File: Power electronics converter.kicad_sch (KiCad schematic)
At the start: 0 parts

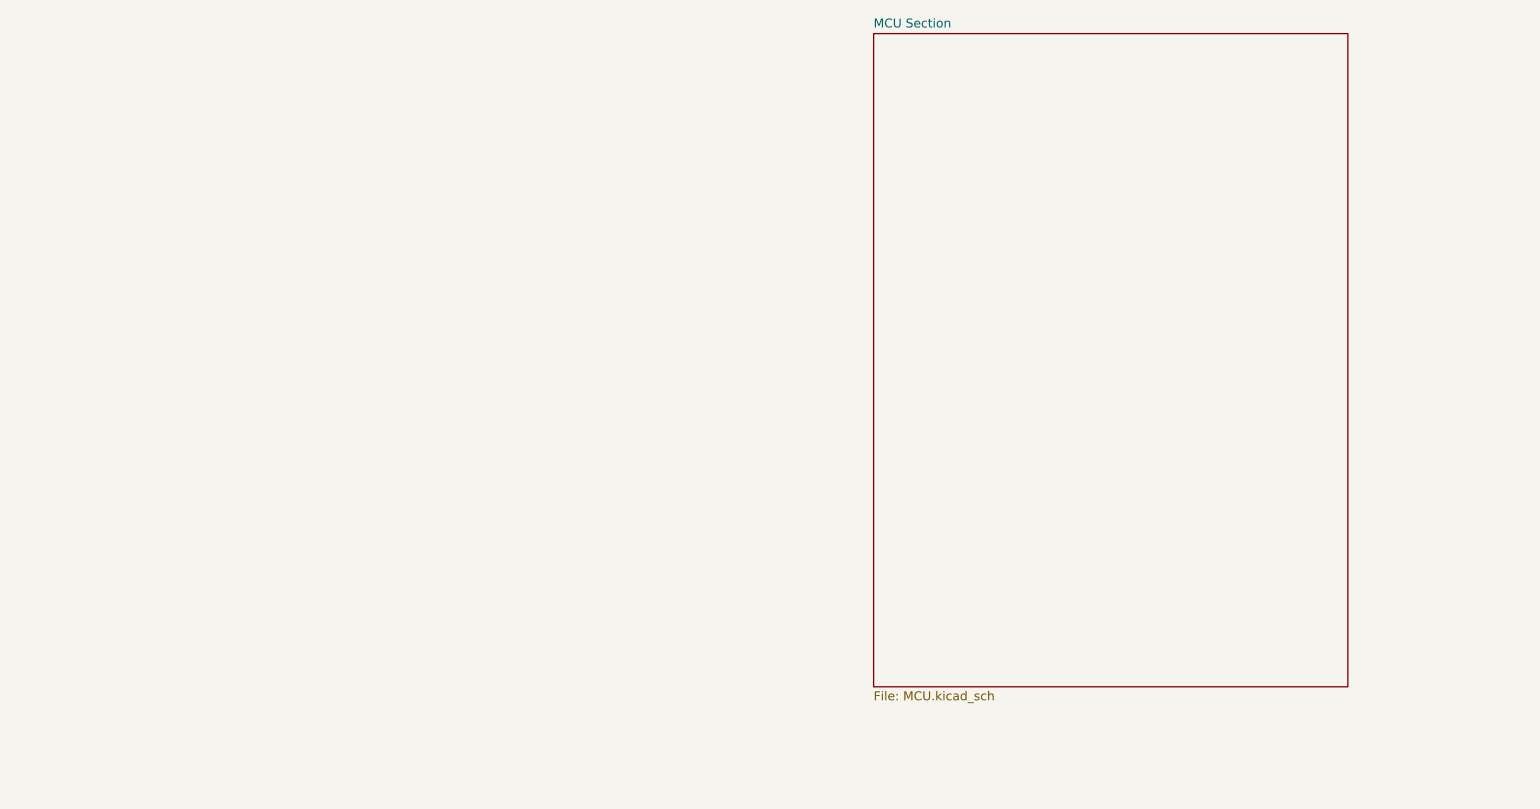
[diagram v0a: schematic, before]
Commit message: Schematic finished pending of layout
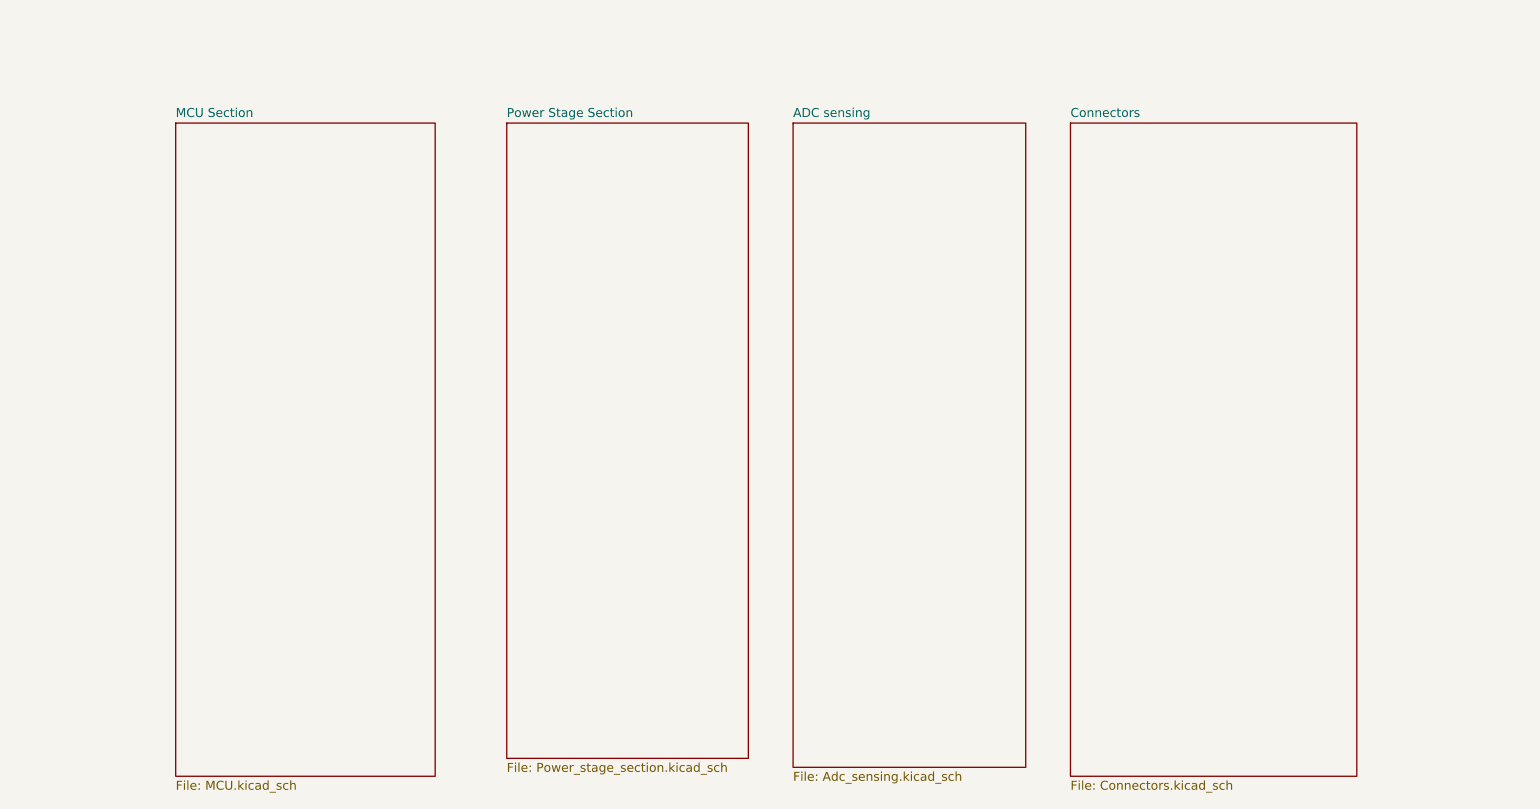
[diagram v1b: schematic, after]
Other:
- added sheet ADC sensing (Adc_sensing.kicad_sch)
- added sheet Connectors (Connectors.kicad_sch)
- added sheet Power Stage Section (Power_stage_section.kicad_sch)
- title: (none) -> SYNCHRONOUS BUCK CONVERTER PROJECT
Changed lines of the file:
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@@
 	(generator_version "9.0")
 	(paper "A4")
+	(title_block
+		(title "SYNCHRONOUS BUCK CONVERTER PROJECT")
+	)
 	(sheet
-		(at 162.56 27.94)
-		(size 67.31 92.71)
+		(at 63.5 40.64)
+		(size 36.83 92.71)
 		(exclude_from_sim no)
 		(in_bom yes)
@@
 		)
 		(property "Sheetname" "MCU Section"
-			(at 162.56 27.2284 0)
+			(at 63.5 39.9284 0)
 			(effects
 				(font
@@
 		)
 		(property "Sheetfile" "MCU.kicad_sch"
-			(at 162.56 121.2346 0)
+			(at 63.5 133.9346 0)
 			(effects
 				(font
@@
 				)
 			)
+		)
+	)
+	(sheet
+		(at 151.13 40.64)
+		(size 33.02 91.44)
+		(exclude_from_sim no)
+		(in_bom yes)
+		(on_board yes)
+		(dnp no)
+		(fields_autoplaced yes)
+		(stroke
+			(width 0.1524)
+			(type solid)
+		)
+		(fill
+			(color 0 0 0 0.0000)
+		)
+		(property "Sheetname" "ADC sensing"
+			(at 151.13 39.9284 0)
+			(effects
+				(font
+					(size 1.27 1.27)
+				)
+				(justify left bottom)
+			)
+		)
+		(property "Sheetfile" "Adc_sensing.kicad_sch"
+			(at 151.13 132.6646 0)
+			(effects
+				(font
+					(size 1.27 1.27)
+				)
+				(justify left top)
+			)
+		)
+		(instances
+			(project "Power electronics converter"
+				(path "/8bff22cb-9bb1-47e8-8b56-bb93bafcd2ef"
+					(page "4")
+				)
+			)
+		)
+	)
+	(sheet
+		(at 190.5 40.64)
+		(size 40.64 92.71)
+		(exclude_from_sim no)
+		(in_bom yes)
+		(on_board yes)
+		(dnp no)
+		(fields_autoplaced yes)
+		(stroke
+			(width 0.1524)
+			(type solid)
+		)
+		(fill
+			(color 0 0 0 0.0000)
+		)
+		(property "Sheetname" "Connectors"
+			(at 190.5 39.9284 0)
+			(effects
+				(font
+					(size 1.27 1.27)
+				)
+				(justify left bottom)
+			)
+		)
+		(property "Sheetfile" "Connectors.kicad_sch"
+			(at 190.5 133.9346 0)
+			(effects
+				(font
+					(size 1.27 1.27)
+				)
+				(justify left top)
+			)
+		)
+		(instances
+			(project "Power electronics converter"
+				(path "/8bff22cb-9bb1-47e8-8b56-bb93bafcd2ef"
+					(page "5")
+				)
+			)
+		)
+	)
+	(sheet
+		(at 110.49 40.64)
+		(size 34.29 90.17)
+		(exclude_from_sim no)
+		(in_bom yes)
+		(on_board yes)
+		(dnp no)
+		(fields_autoplaced yes)
+		(stroke
+			(width 0.1524)
+			(type solid)
+		)
+		(fill
+			(color 0 0 0 0.0000)
+		)
+		(property "Sheetname" "Power Stage Section"
+			(at 110.49 39.9284 0)
+			(effects
+				(font
+					(size 1.27 1.27)
+				)
+				(justify left bottom)
+			)
+		)
+		(property "Sheetfile" "Power_stage_section.kicad_sch"
+			(at 110.49 131.3946 0)
+			(effects
+				(font
+					(size 1.27 1.27)
+				)
+				(justify left top)
+			)
+		)
+		(instances
+			(project "Power electronics converter"
+				(path "/8bff22cb-9bb1-47e8-8b56-bb93bafcd2ef"
+					(page "3")
+				)
+			)

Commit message: over-voltage protection added
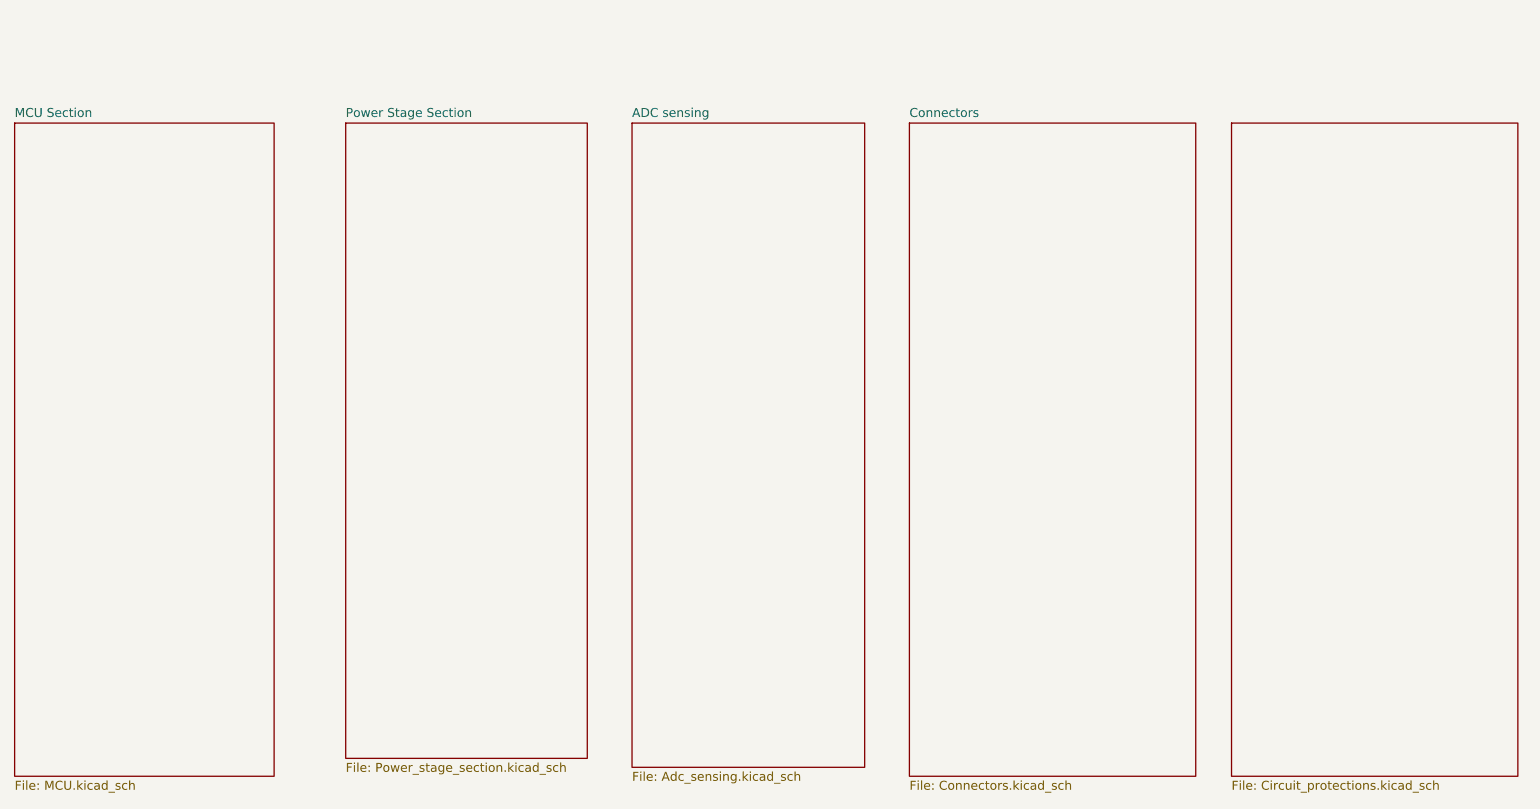
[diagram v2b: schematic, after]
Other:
- added sheet Circuit_protections (Circuit_protections.kicad_sch)
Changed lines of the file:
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@@
 	)
 	(sheet
-		(at 63.5 40.64)
+		(at 40.64 40.64)
 		(size 36.83 92.71)
 		(exclude_from_sim no)
@@
 		)
 		(property "Sheetname" "MCU Section"
-			(at 63.5 39.9284 0)
+			(at 40.64 39.9284 0)
 			(effects
 				(font
@@
 		)
 		(property "Sheetfile" "MCU.kicad_sch"
-			(at 63.5 133.9346 0)
+			(at 40.64 133.9346 0)
 			(effects
 				(font
@@
 	)
 	(sheet
-		(at 151.13 40.64)
+		(at 128.27 40.64)
 		(size 33.02 91.44)
 		(exclude_from_sim no)
@@
 		)
 		(property "Sheetname" "ADC sensing"
-			(at 151.13 39.9284 0)
+			(at 128.27 39.9284 0)
 			(effects
 				(font
@@
 		)
 		(property "Sheetfile" "Adc_sensing.kicad_sch"
-			(at 151.13 132.6646 0)
+			(at 128.27 132.6646 0)
 			(effects
 				(font
@@
 	)
 	(sheet
-		(at 190.5 40.64)
+		(at 167.64 40.64)
 		(size 40.64 92.71)
 		(exclude_from_sim no)
@@
 		)
 		(property "Sheetname" "Connectors"
-			(at 190.5 39.9284 0)
+			(at 167.64 39.9284 0)
 			(effects
 				(font
@@
 		)
 		(property "Sheetfile" "Connectors.kicad_sch"
-			(at 190.5 133.9346 0)
+			(at 167.64 133.9346 0)
 			(effects
 				(font
@@
 	)
 	(sheet
-		(at 110.49 40.64)
+		(at 87.63 40.64)
 		(size 34.29 90.17)
 		(exclude_from_sim no)
@@
 		)
 		(property "Sheetname" "Power Stage Section"
-			(at 110.49 39.9284 0)
+			(at 87.63 39.9284 0)
 			(effects
 				(font
@@
 		)
 		(property "Sheetfile" "Power_stage_section.kicad_sch"
-			(at 110.49 131.3946 0)
+			(at 87.63 131.3946 0)
 			(effects
 				(font
@@
 				)
 			)
+		)
+	)
+	(sheet
+		(at 213.36 40.64)
+		(size 40.64 92.71)
+		(exclude_from_sim no)
+		(in_bom yes)
+		(on_board yes)
+		(dnp no)
+		(fields_autoplaced yes)
+		(stroke
+			(width 0.1524)
+			(type solid)
+		)
+		(fill
+			(color 0 0 0 0.0000)
+		)
+		(property "Sheetname" "Circuit_protections"
+			(at 213.36 39.9284 0)
+			(effects
+				(font
+					(size 1.27 1.27)
+				)
+				(justify left bottom)
+				(hide yes)
+			)
+		)
+		(property "Sheetfile" "Circuit_protections.kicad_sch"
+			(at 213.36 133.9346 0)
+			(effects
+				(font
+					(size 1.27 1.27)
+				)
+				(justify left top)
+			)
+		)
+		(property "Field2" ""
+			(at 213.36 40.64 0)
+			(effects
+				(font
+					(size 1.27 1.27)
+				)
+			)
+		)
+		(instances
+			(project "Power electronics converter"
+				(path "/8bff22cb-9bb1-47e8-8b56-bb93bafcd2ef"
+					(page "6")
+				)
+			)
